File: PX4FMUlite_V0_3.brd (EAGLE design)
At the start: 48.6 x 34.9 mm, 142 parts, among them J2 DF13-4P-1.25V, J201 DF13C-6P-1.25V, J202 DF13C-6P-1.25V, J203 DF13C-6P-1.25V, J3 DF13C-4P-1.25V, J302 DF13C-4P-1.25V, J401 DF13C-4P-1.25V, J403 DF13C-7P-1.25V, J405 DF13C-4P-1.25V, J802 DF13C-3P-1.25V, M3_MOUNT1101 MOUNT-HOLE3.1MM, M3_MOUNT1102 MOUNT-HOLE3.1MM, M3_MOUNT1103 MOUNT-HOLE3.1MM, M3_MOUNT1104 MOUNT-HOLE3.1MM, U101 STM32F4X7VX, U2 MAX3051, U401 MAX3051, X101 3.2x2.5 mm / 24 MHz / 15 ppm

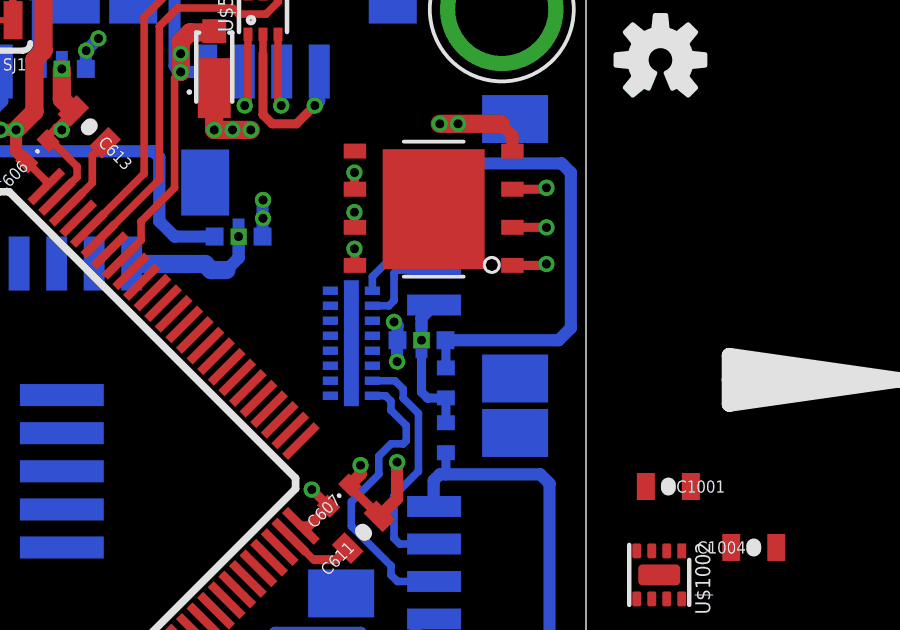
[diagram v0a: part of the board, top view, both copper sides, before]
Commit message: Flash power decoupling
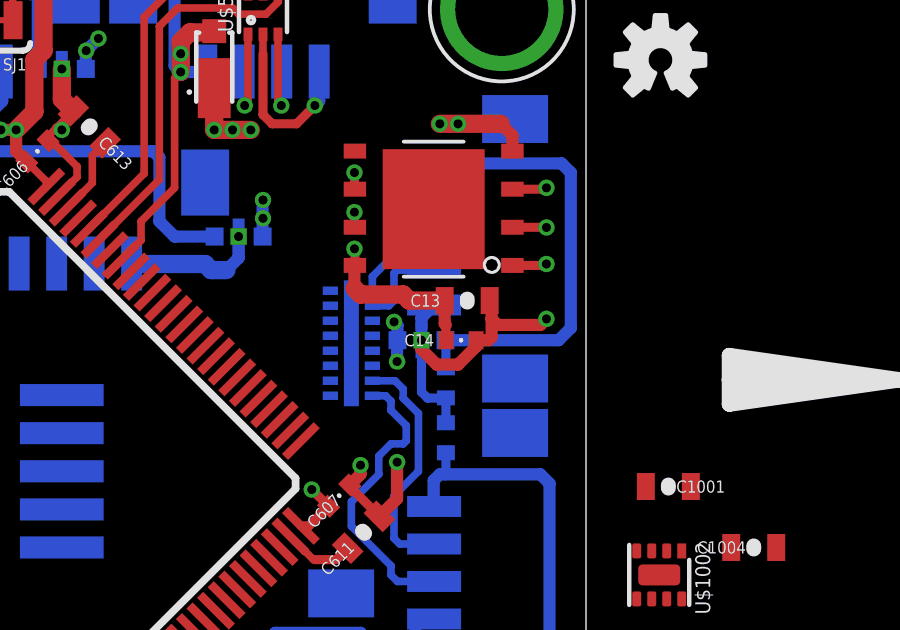
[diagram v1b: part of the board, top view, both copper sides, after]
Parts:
- added C13: 2u2, pixhawk2:0603-CAP
- added C14: 0u1, pixhawk2:0402-CAP
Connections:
- net FMU-VDD_3V3: now also C13.P$1, C14.P$1
- net GND: now also C13.P$2, C14.P$2
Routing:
- net GND: track 136.3 -> 142.9 mm, vias 34 -> 35
- net FMU-VDD_3V3: track 64.9 -> 70.2 mm

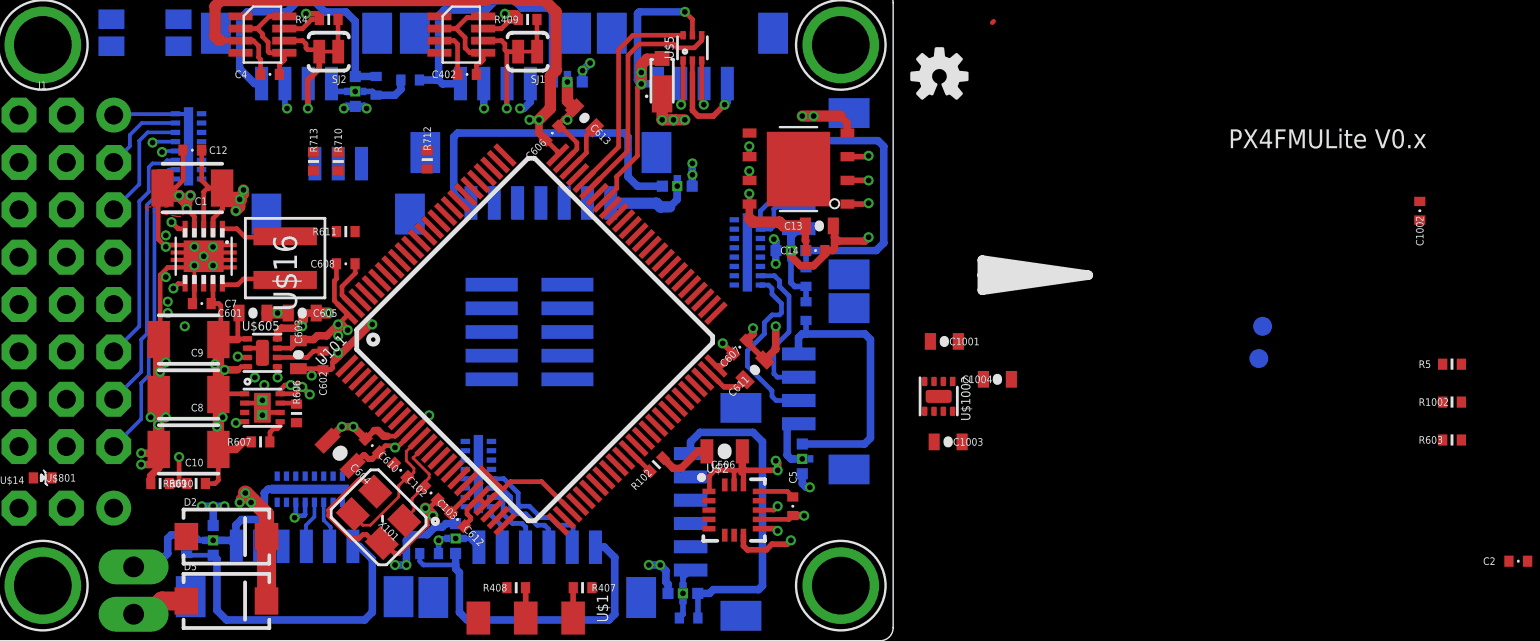
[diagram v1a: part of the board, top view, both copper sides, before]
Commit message: Sensor LDO routed
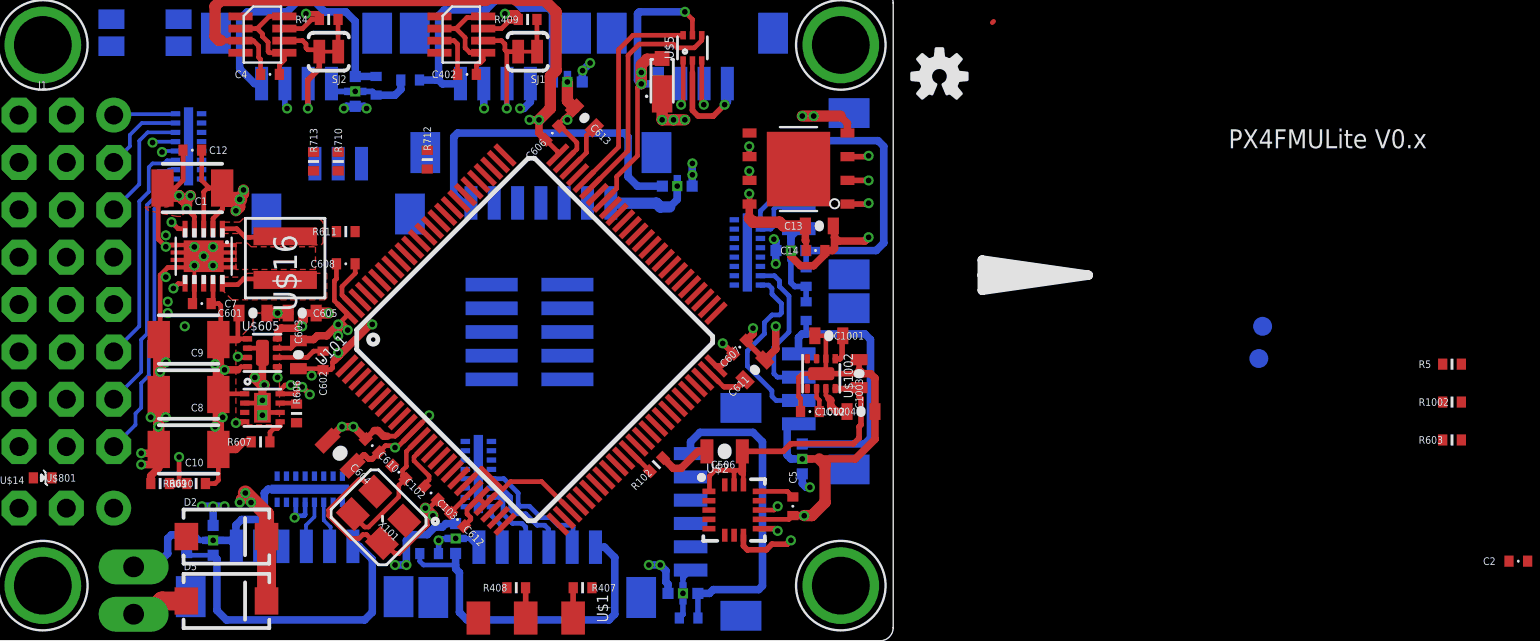
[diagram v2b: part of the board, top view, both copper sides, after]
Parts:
- moved C1002 34.4 mm to (53.3, 15.0), turned to 180 degrees
- moved C1004 7.52 mm to (56.1, 15.0)
- moved U$1002 6.42 mm to (53.9, 17.1)
- moved C1001 6.21 mm to (54.4, 19.1)
- moved C1003 6.02 mm to (56.0, 17.1), turned to 90 degrees
- moved C102 0.14 mm to (31.3, 11.8)
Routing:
- net GND: track 142.9 -> 168.8 mm
- net VDD_3V3_SENSORS: track 9.48 -> 16.0 mm, vias 2 -> 0
- net N$1: track 5.48 -> 2.93 mm
- net VDD_3V3_PERIPH: track 0.00 -> 2.04 mm
- net VDD_5V: track 23.2 -> 25.0 mm
- net N$104: track 0.00 -> 1.30 mm
- net FMU-CH1-PROT: track 4.51 -> 3.34 mm
- added copper zone on layer 1, net N$10
- added copper zone on layer 1, net N$17

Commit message: More stuff
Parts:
- added C15: 0u1, pixhawk2:0402-CAP
- moved R2 56.2 mm to (50.3, 21.2), flipped to the top
- moved C2 53.0 mm to (38.3, 6.71)
- moved C3 52.7 mm to (40.5, 6.71)
- moved R1 51.4 mm to (50.3, 22.4), flipped to the top
- moved R401 49.1 mm to (50.0, 24.6), turned to 0 degrees
- moved R402 49.1 mm to (50.0, 23.5), turned to 0 degrees
- moved C505 43.3 mm to (51.4, 12.2)
- moved R707 8.32 mm to (15.0, 43.1)
- moved R610 0.10 mm to (18.4, 11.2)
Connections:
- net FMU-VDD_3V3: now also C15.P$1
- net GND: now also C15.P$2
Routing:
- net VDD_5V: track 25.0 -> 87.1 mm, vias 4 -> 8
- net GND: track 168.8 -> 181.1 mm
- net FMU-VDD_3V3: track 70.2 -> 76.1 mm
- net FMU-I2C1_SDA: track 0.00 -> 2.39 mm, vias 0 -> 1
- net FMU-I2C2_SCL: track 0.00 -> 2.07 mm, vias 0 -> 1
- net FMU-I2C1_SCL: track 0.00 -> 2.00 mm, vias 0 -> 1
- net SAFETY: track 0.00 -> 1.91 mm, vias 0 -> 1
- net N$57: track 0.00 -> 1.85 mm, vias 0 -> 1
- net FMU_AUX_ADC2_PROT: track 1.63 -> 2.98 mm
- net VDD_3V3_SENSORS: track 16.0 -> 17.4 mm
- net FMU-I2C2_SDA: track 0.00 -> 1.25 mm, vias 0 -> 1
- net FMU_AUX_ADC1_PROT: track 1.63 -> 2.88 mm
- net !GYRO_CS: track 4.82 -> 3.85 mm

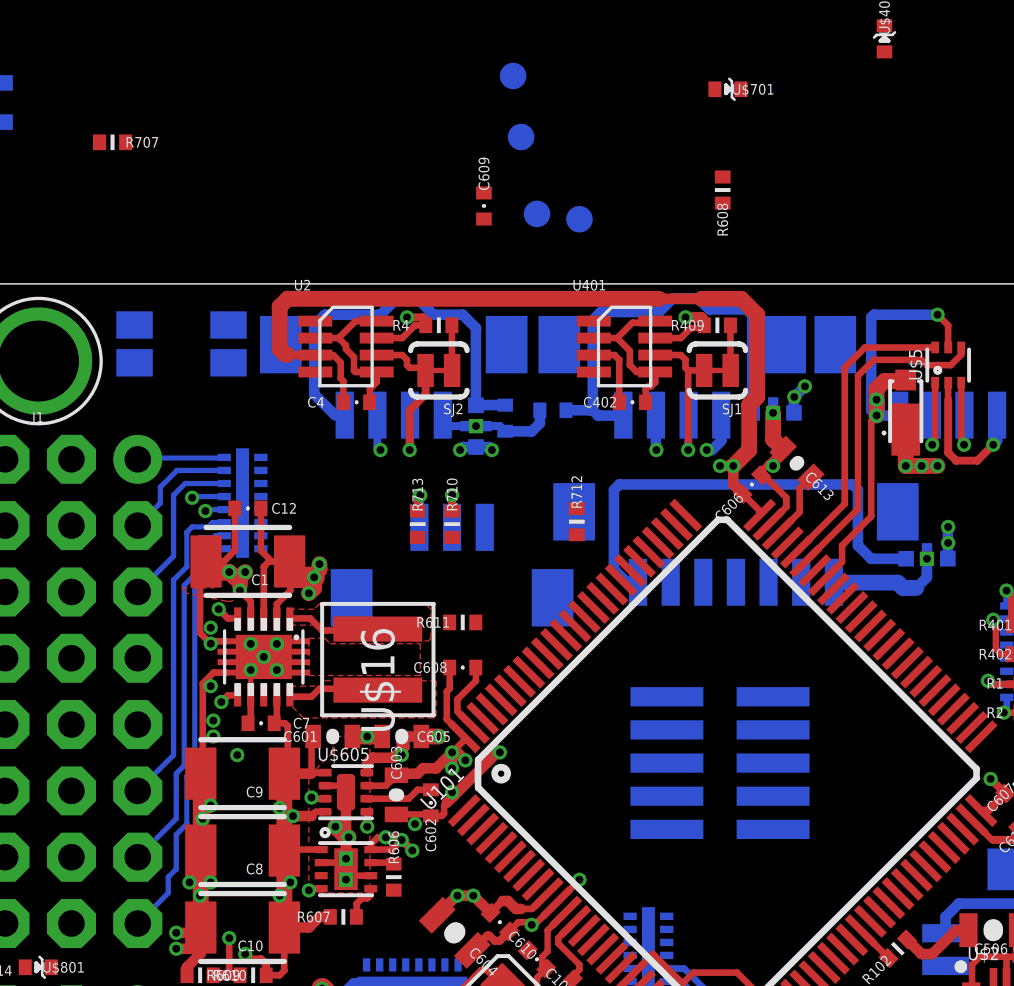
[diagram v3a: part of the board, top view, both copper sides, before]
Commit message: VDD_5V_PERIPH and GND powerplanes added
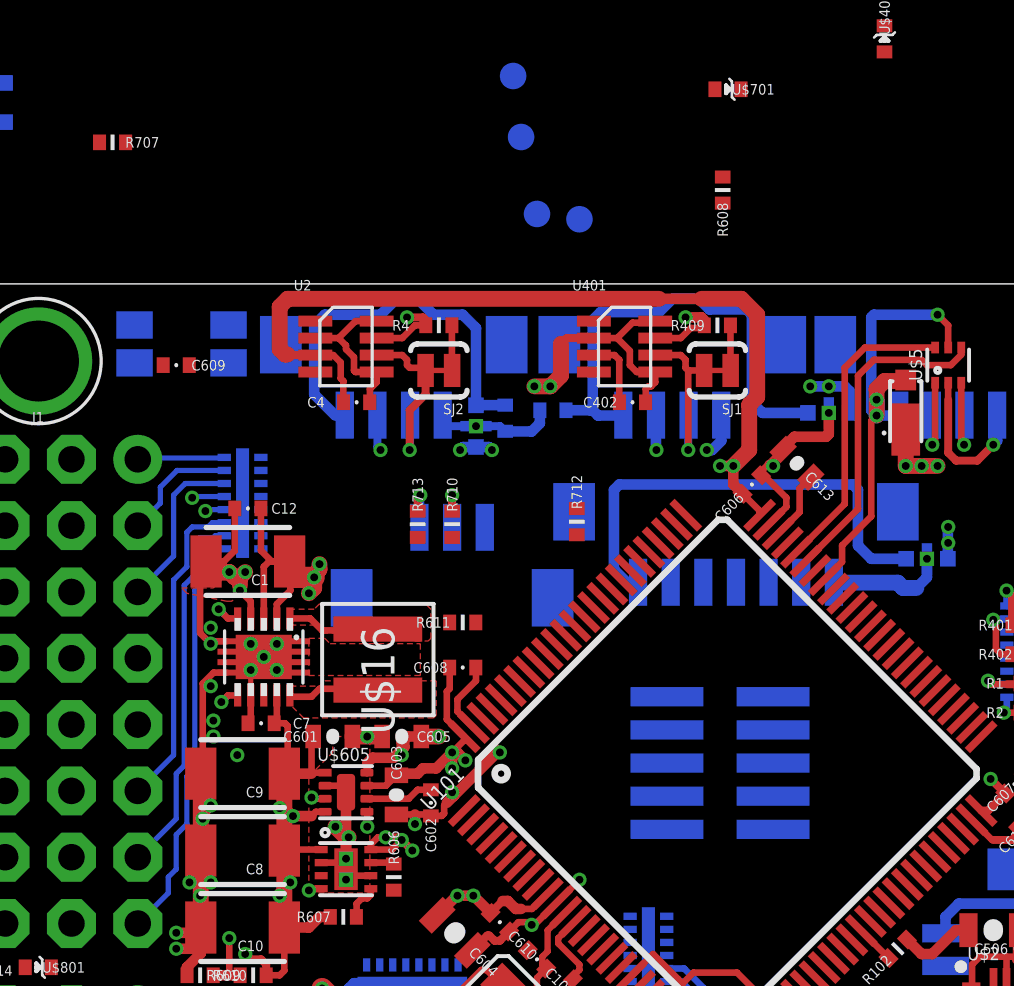
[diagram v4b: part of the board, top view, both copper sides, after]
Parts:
- moved C609 13.3 mm to (17.5, 34.5), turned to 180 degrees
- moved L403 2.13 mm to (42.5, 32.7)
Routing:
- net GND: track 181.1 -> 186.5 mm, vias 35 -> 37
- net VDD_5V_PERIPH: track 89.2 -> 91.4 mm
- net N$48: track 16.2 -> 18.2 mm
- net VDD_IN: track 69.9 -> 70.9 mm
- added copper zone on layer 15, net VDD_5V_PERIPH

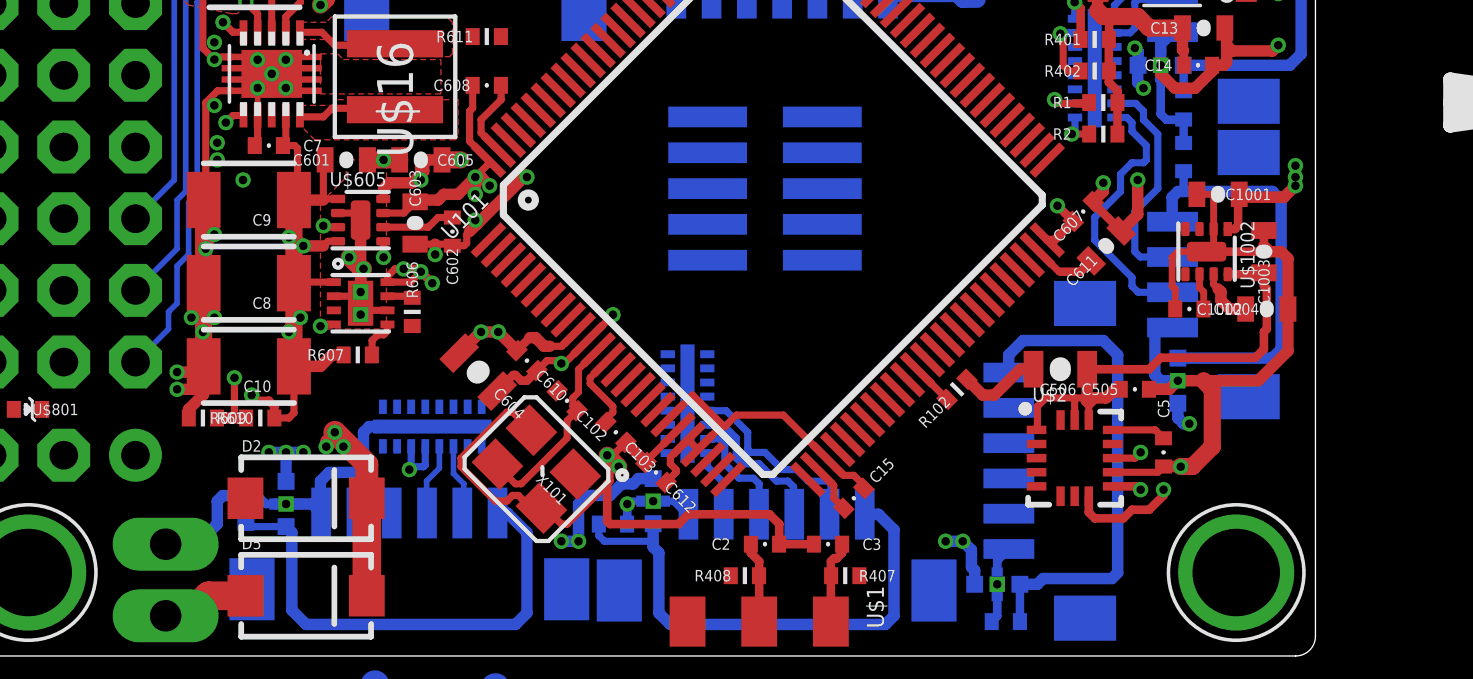
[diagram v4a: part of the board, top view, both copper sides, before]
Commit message: Rerouting of 5V_IN to improve V_SERVO routing
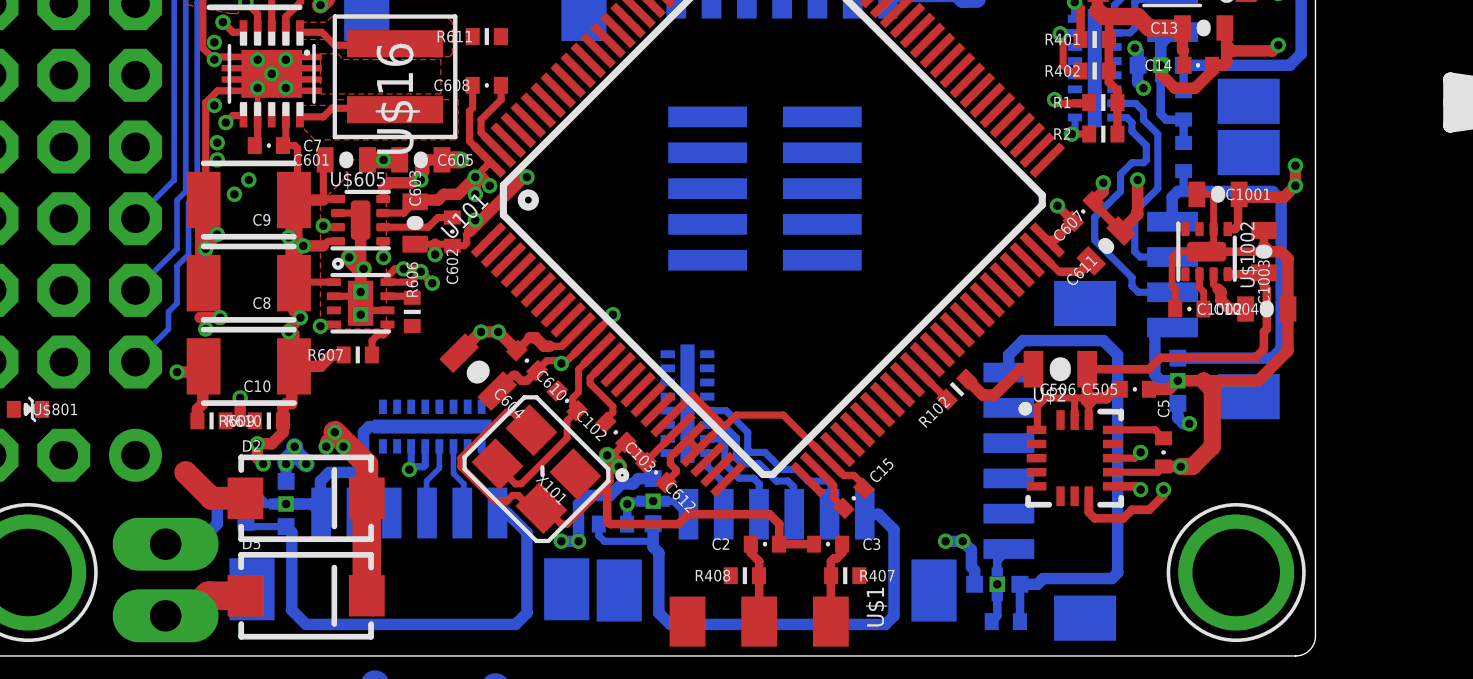
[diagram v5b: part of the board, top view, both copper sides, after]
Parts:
- moved R609 0.32 mm to (20.7, 11.1)
- moved R610 0.32 mm to (18.7, 11.1)
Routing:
- net VDD_3V3_SPEKTRUM: track 28.9 -> 44.7 mm, vias 3 -> 4
- net VDD_5V: track 87.1 -> 82.1 mm
- net GND: track 186.5 -> 182.0 mm, vias 37 -> 35
- net VDD_5V_PERIPH: track 91.4 -> 87.3 mm
- net V_SERVO: track 0.00 -> 2.50 mm
- net VDD_5V_SENS: track 2.87 -> 1.84 mm
- net N$18: track 15.5 -> 16.4 mm
